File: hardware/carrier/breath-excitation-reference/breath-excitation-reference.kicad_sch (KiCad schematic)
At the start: 11 parts

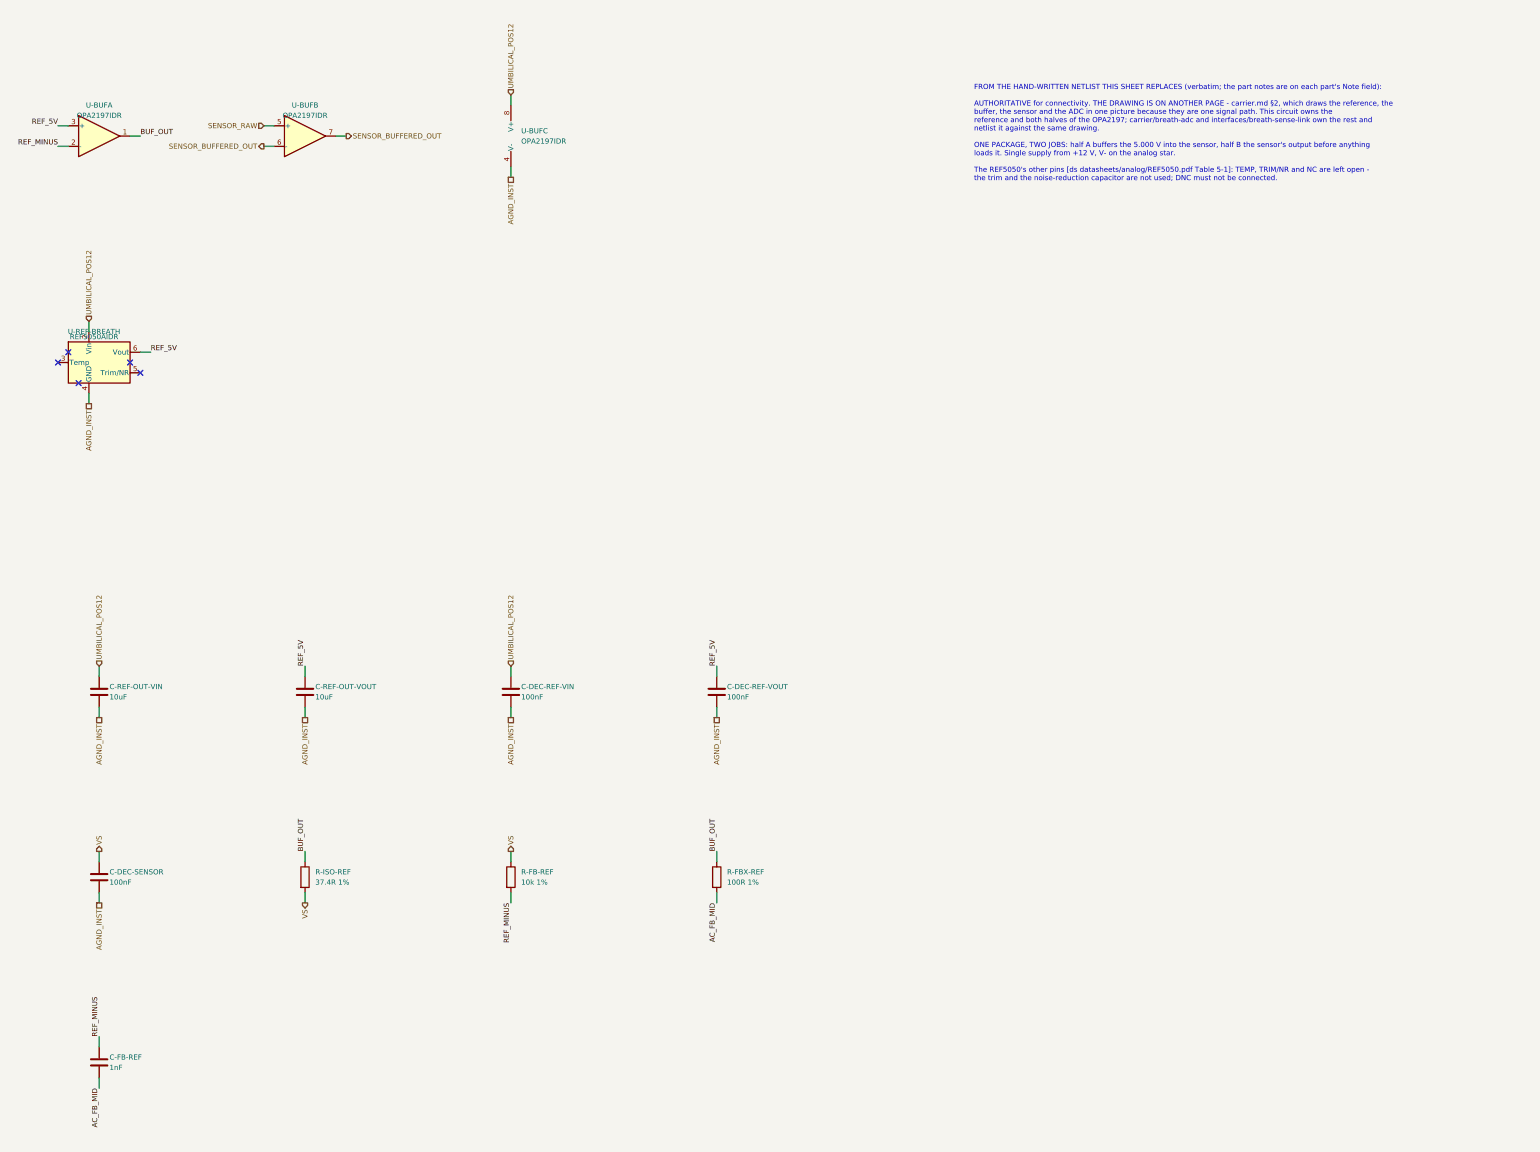
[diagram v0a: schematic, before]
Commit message: Clamp the REF5050's input; bank the main board's chosen-part datasheets
The rail's TVS clamps at up to 24.4 V, and the REF5050's VIN absolute maximum
is 18 V. The reference is now fed through R-REF-IN (330R) and held by
D-REF-CLAMP (MMSZ5245B 15 V zener) on a new REF_VIN node. At the TVS clamp
the zener holds VIN at about 16.1 V or less. In normal running the drop is
0.4 V.

- The breath-excitation-reference sheet is rebuilt from its netlist and
  re-exported, with a PWR_FLAG on REF_VIN.
- The page gains a derivation section, and carrier.md's drawing shows the
  clamp.
- The main board re-places the sheets; the reference table is regenerated.
  R and D references after the new parts shift by one.
- Board ERC is clean, and key-board fab is re-rendered (fingerprints only).
- Fragments R24/R25 bank the parts agents' datasheets, 196 verified.

Co-Authored-By: Claude Opus 5.5 <noreply@anthropic.com>
Claude-Session: https://claude.ai/code/session_01LmB4muFXnoLprWX4JzuJ5A
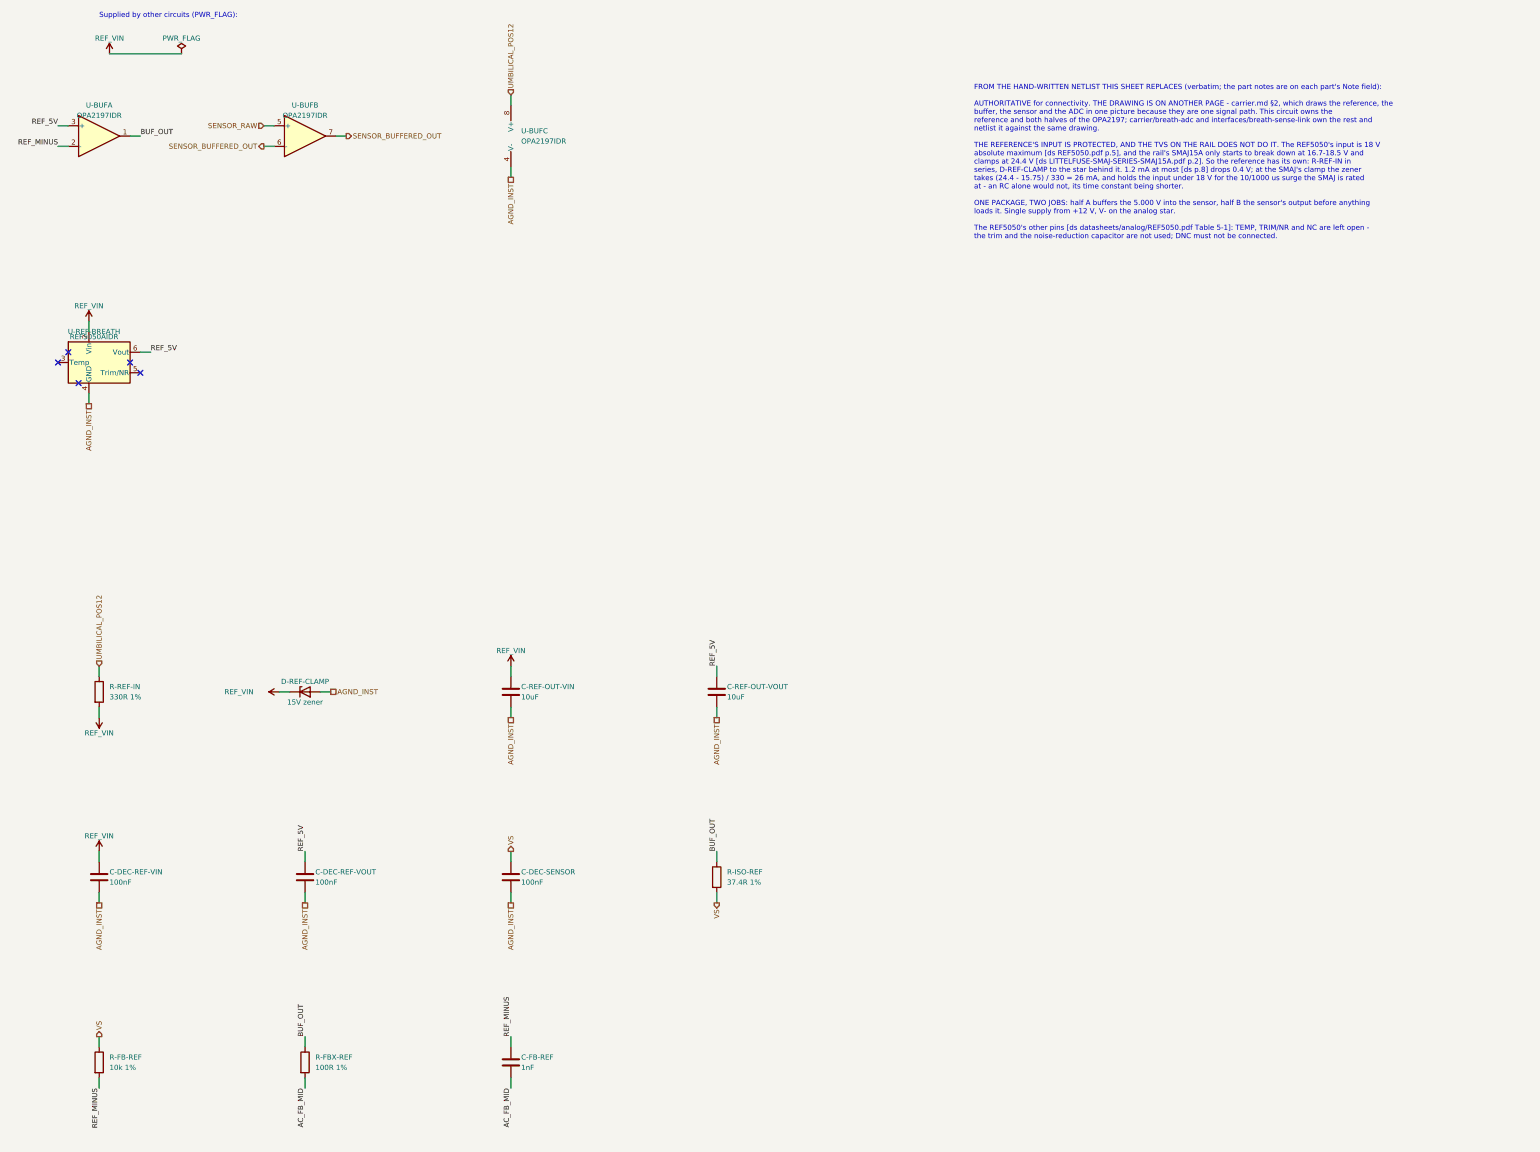
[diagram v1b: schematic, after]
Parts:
- added D-REF-CLAMP: 15V zener, symbol Device:D_Zener
- added R-REF-IN: 330R 1%, symbol Device:R
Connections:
- net AGND_INST: now also D-REF-CLAMP.2 (A)
- net UMBILICAL_POS12: now also R-REF-IN.1; no longer C-DEC-REF-VIN.1, C-REF-OUT-VIN.1, U-REF-BREATH.2 (Vin)
- new net REF_VIN: C-DEC-REF-VIN.1, C-REF-OUT-VIN.1, D-REF-CLAMP.1 (K), R-REF-IN.2, U-REF-BREATH.2 (Vin)
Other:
- note added: "Supplied by other circuits (PWR_FLAG):"
- moved on the sheet: C-DEC-REF-VIN, C-DEC-REF-VOUT, C-DEC-SENSOR, C-FB-REF, C-REF-OUT-VIN, C-REF-OUT-VOUT, R-FB-REF, R-FBX-REF, R-ISO-REF

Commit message: Main board: apply the chosen parts to every symbol and row
Every main-board and adapter symbol now carries Footprint, Manufacturer,
MPN, LCSC and Assembly. The values come from the selections whose
datasheets are banked. The BOM rows follow those choices:

- D-USBOR is the SS14 (SMA).
- J-LED is four solder pads, not a connector.
- L-BUCK-IN is 22 uH, C-BUCK-IN is a UCM electrolytic, C-STRIP-BULK is
  470 uF 25 V.
- D-TVS-BREATH is the PESD12VS1UA (SOD-323); the UB is SOD523.
- J-UMB is the hanxia header. Its posts go through the adapter and its
  tails through the tongue; the old wording had them swapped.
- U-BUCK and U-BREATH say where to buy.
- C-ADC-BULK is 1206 if fitted.

The body and geometry follow the chosen parts:

- The J-UMB and J-MCU envelopes in config/body.yaml are now read off the
  parts' drawings.
- J-MCU is longer, so the regulator block moved and the right-hand ribbon
  header followed it by 1.5 mm. The RH key board is re-laid out, with C8
  moving with the header's 3V3 pin. It checks clean.
- A mount candidate is now nudged by up to 3 mm before it is dropped. All
  seven main-board mounts hold.

New footprints and pages:

- New woody.pretty footprints: the MPXV4006DP (case 1351-01) from
  breath-sense-link.md's land pattern, and the NE8FAV from Neutrik's
  layout, mirrored to the top view.
- The input-LC derivation uses the chosen capacitor's banked ESR: Q is at
  most 1.8, and the margin is 120x worst case.
- The main-board README lists what is still open before layout.

Co-Authored-By: Claude Opus 5.5 <noreply@anthropic.com>
Claude-Session: https://claude.ai/code/session_01LmB4muFXnoLprWX4JzuJ5A
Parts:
- C-DEC-REF-VIN, C-DEC-REF-VOUT, C-DEC-SENSOR: footprint (none) -> Capacitor_SMD:C_0805_2012Metric; Assembly (none) -> machine; LCSC (none) -> C49678; MPN (none) -> CC0805KRX7R9BB104; Manufacturer (none) -> YAGEO
- C-FB-REF: footprint (none) -> Capacitor_SMD:C_0805_2012Metric; Assembly (none) -> machine; LCSC (none) -> C62774; MPN (none) -> CC0805JRNPO9BN102; Manufacturer (none) -> YAGEO
- C-REF-OUT-VIN, C-REF-OUT-VOUT: footprint (none) -> Capacitor_SMD:C_1206_3216Metric; Assembly (none) -> machine; LCSC (none) -> C89632; MPN (none) -> CL31B106KBHNNNE; Manufacturer (none) -> Samsung Electro-Mechanics
- D-REF-CLAMP: footprint (none) -> Diode_SMD:D_SOD-123; Assembly (none) -> machine; LCSC (none) -> C129730; MPN (none) -> MMSZ5245BT1G; Manufacturer (none) -> onsemi
- R-FB-REF: footprint (none) -> Resistor_SMD:R_0805_2012Metric; Assembly (none) -> machine; LCSC (none) -> C17414; MPN (none) -> 0805W8F1002T5E; Manufacturer (none) -> UNI-ROYAL
- R-FBX-REF: footprint (none) -> Resistor_SMD:R_0805_2012Metric; Assembly (none) -> machine; LCSC (none) -> C17408; MPN (none) -> 0805W8F1000T5E; Manufacturer (none) -> UNI-ROYAL
- R-ISO-REF: footprint (none) -> Resistor_SMD:R_0805_2012Metric; Assembly (none) -> machine; LCSC (none) -> C204458; MPN (none) -> CR0805-FX-37R4ELF; Manufacturer (none) -> Bourns
- R-REF-IN: footprint (none) -> Resistor_SMD:R_0805_2012Metric; Assembly (none) -> machine; LCSC (none) -> C17630; MPN (none) -> 0805W8F3300T5E; Manufacturer (none) -> UNI-ROYAL
- U-BUF: footprint (none) -> Package_SO:SOIC-8_3.9x4.9mm_P1.27mm; Assembly (none) -> machine; LCSC (none) -> C139363; MPN (none) -> OPA2197IDR; Manufacturer (none) -> Texas Instruments
- U-REF-BREATH: footprint (none) -> Package_SO:SOIC-8_3.9x4.9mm_P1.27mm; Assembly (none) -> machine; LCSC (none) -> C27804; MPN (none) -> REF5050AIDR; Manufacturer (none) -> Texas Instruments

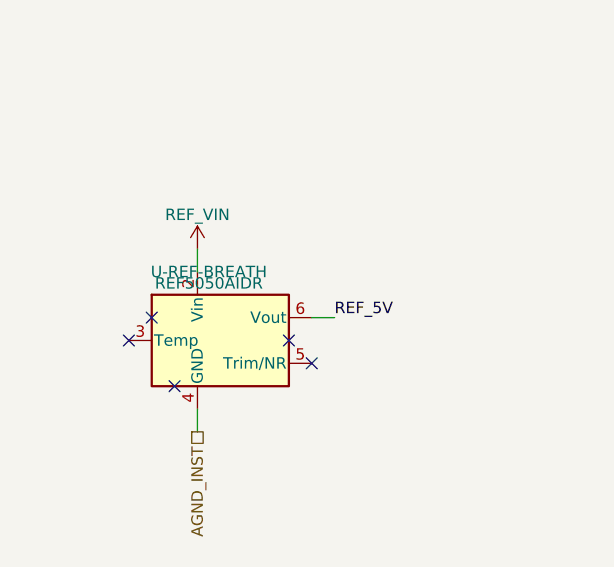
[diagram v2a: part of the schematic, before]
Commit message: ref5050-grade settled: REF5050IDR, the High grade (sheet, BOM, figure, ADR 0003)
The A suffix is TI's Standard grade (SBOS410O Table 4-2); the reference
exists only for scale-factor stability, so the order code loses the A.
Same SOIC-8 pinout. LCSC C24696, in stock 2026-09-30.

Co-Authored-By: Claude Opus 5.5 <noreply@anthropic.com>
Claude-Session: https://claude.ai/code/session_01LmB4muFXnoLprWX4JzuJ5A
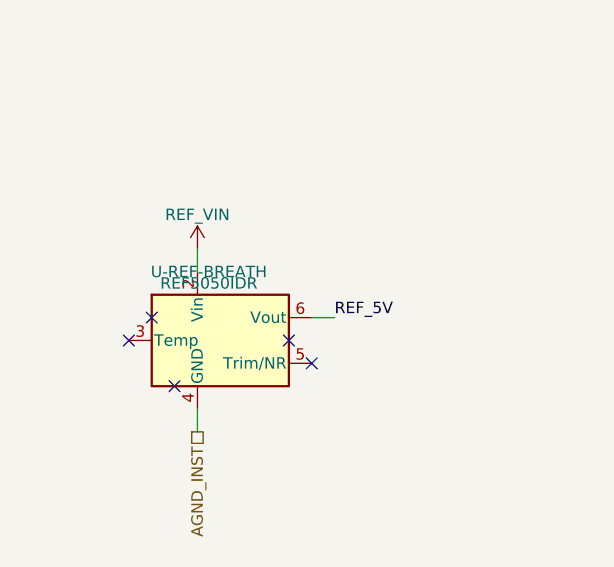
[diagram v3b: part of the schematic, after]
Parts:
- U-REF-BREATH: value REF5050AIDR -> REF5050IDR; LCSC C27804 -> C24696; MPN REF5050AIDR -> REF5050IDR; Pins_source datasheets/analog/REF5050.pdf section 5, Table 5-1 (REF50xxAI, SOIC-8) -> datasheets/analog/REF5050.pdf section 5, Table 5-1 (REF50xxI, SOIC-8: the same pins as REF50xxAI)
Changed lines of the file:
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@@
     (in_bom yes) (on_board yes) (dnp no)
     (property "Reference" "U-REF-BREATH" (at 39.37 99.06 0) (effects (font (size 1.27 1.27))))
-    (property "Value" "REF5050AIDR" (at 39.37 100.33 0) (effects (font (size 1.27 1.27))))
+    (property "Value" "REF5050IDR" (at 39.37 100.33 0) (effects (font (size 1.27 1.27))))
     (property "Footprint" "Package_SO:SOIC-8_3.9x4.9mm_P1.27mm" (at 38.1 113.03 0) (effects (font (size 1.27 1.27)) hide))
     (property "Datasheet" "" (at 39.37 106.68 0) (effects (font (size 1.27 1.27)) hide))
@@
     (property "Drawn_as" "REF5050" (at 40.64 106.68 0) (effects (font (size 1.27 1.27)) hide))
     (property "Note" "5.000 V, and it is the excitation's absolute accuracy - the sensor is ratiometric, so every volt of error here is a volt of error at the jack" (at 40.64 106.68 0) (effects (font (size 1.27 1.27)) hide))
-    (property "Pins_source" "datasheets/analog/REF5050.pdf section 5, Table 5-1 (REF50xxAI, SOIC-8)" (at 40.64 106.68 0) (effects (font (size 1.27 1.27)) hide))
+    (property "Pins_source" "datasheets/analog/REF5050.pdf section 5, Table 5-1 (REF50xxI, SOIC-8: the same pins as REF50xxAI)" (at 40.64 106.68 0) (effects (font (size 1.27 1.27)) hide))
     (property "Manufacturer" "Texas Instruments" (at 40.64 106.68 0) (effects (font (size 1.27 1.27)) hide))
-    (property "MPN" "REF5050AIDR" (at 40.64 106.68 0) (effects (font (size 1.27 1.27)) hide))
-    (property "LCSC" "C27804" (at 40.64 106.68 0) (effects (font (size 1.27 1.27)) hide))
+    (property "MPN" "REF5050IDR" (at 40.64 106.68 0) (effects (font (size 1.27 1.27)) hide))
+    (property "LCSC" "C24696" (at 40.64 106.68 0) (effects (font (size 1.27 1.27)) hide))
     (property "Assembly" "machine" (at 40.64 106.68 0) (effects (font (size 1.27 1.27)) hide))
     (pin "1")

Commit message: Breath ADC and reference: C-ADC-BULK fitted, no series R on C-REF-OUT, ADC provenance from DS21034F
C-ADC-BULK fitted as the reference pin's reservoir; the PWM question it was
proposed for is not what it can filter, so E9's scope test is specified on
the page. C-REF-OUT takes no series resistor (SBOS410O 9.4.1.1: optional;
noise peaking stays >100x below an LSB). The MCP3202's clamp-current claim
now cites the datasheet, which rates no injection current at all.

Co-Authored-By: Claude Opus 5.5 <noreply@anthropic.com>
Claude-Session: https://claude.ai/code/session_01LmB4muFXnoLprWX4JzuJ5A
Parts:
- C-REF-OUT-VOUT: Note VOUT load capacitor, on the REF5050's own output -> VOUT load capacitor, on the REF5050's own output, straight 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
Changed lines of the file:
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@@
     (property "Row" "C-REF-OUT" (at 193.04 187.96 0) (effects (font (size 1.27 1.27)) hide))
     (property "Pins" "1=1 2=2" (at 193.04 187.96 0) (effects (font (size 1.27 1.27)) hide))
-    (property "Note" "VOUT load capacitor, on the REF5050's own output" (at 193.04 187.96 0) (effects (font (size 1.27 1.27)) hide))
+    (property "Note" "VOUT load capacitor, on the REF5050's own output, straight to AGND_INST: no series resistor (SBOS410O 9.4.1.1 p.29, optional; see the C-REF-OUT row)" (at 193.04 187.96 0) (effects (font (size 1.27 1.27)) hide))
     (property "Manufacturer" "Samsung Electro-Mechanics" (at 193.04 187.96 0) (effects (font (size 1.27 1.27)) hide))
     (property "MPN" "CL31B106KBHNNNE" (at 193.04 187.96 0) (effects (font (size 1.27 1.27)) hide))
